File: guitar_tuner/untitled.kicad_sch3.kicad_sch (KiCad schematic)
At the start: 0 parts

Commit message: Created the audio input circuit, added all passives and assigned values
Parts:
- added C10: 470nF, symbol Device:C_Small
- added C11: 2.2uF, symbol Device:C_Small
- added C12: 10uF, symbol Device:C_Small
- added C7: 1uF, symbol Device:C_Small
- added C8: .47uF, symbol Device:C_Small
- added C9: .1uF, symbol Device:C_Small
- added MK1: Microphone, symbol Device:Microphone
- added R6: 2.21k, symbol Device:R_Small
- added R7: 150k, symbol Device:R_Small
- added R8: 100k, symbol Device:R_Small
- added R9: 1M, symbol Device:R_Small
- added U3: MAX9814, Package_DFN_QFN:DFN-14-1EP_3x3mm_P0.4mm_EP1.78x2.35mm, symbol Amplifier_Audio:MAX9814
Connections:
- new net: R6.1, R7.1, U3.13 (MICBIAS)
- new net: R7.2, R8.1, U3.14 (TH)
- new net: C10.1, U3.1 (CT)
- new net: C11.2, U3.3 (CG)
- new net: C8.2, U3.12 (BIAS)
- new net: C9.2, MK1.2 (+), R6.2
- new net: C12.1, U3.6 (MICOUT)
- new net: C9.1, U3.8 (MICIN)
- new net GND: C10.2, C11.1, C7.1, C8.1, MK1.1 (-), R8.2, R9.1, U3.11 (GND), U3.15 (GND), U3.4 (GND), U3.7 (GND), U3.9 (A/R)
- new net Vin: C7.2, U3.10 (GAIN), U3.2 (~{SHDN}), U3.5 (VDD)
- new net Vout: C12.2, R9.2

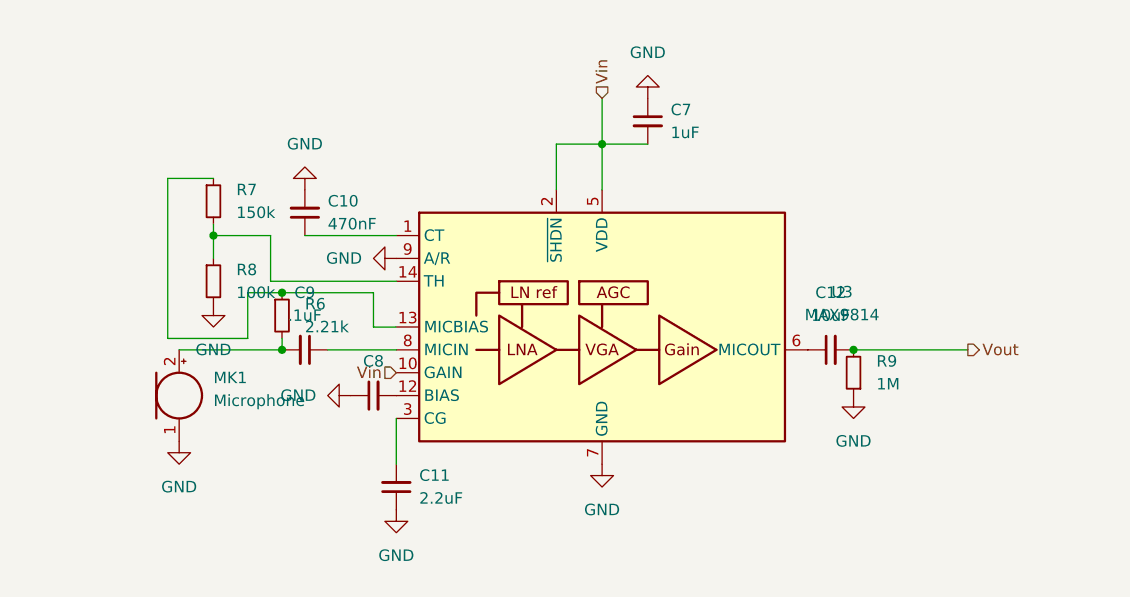
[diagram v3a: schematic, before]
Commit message: Fixed short short with R1 and space out schematic for audio input.
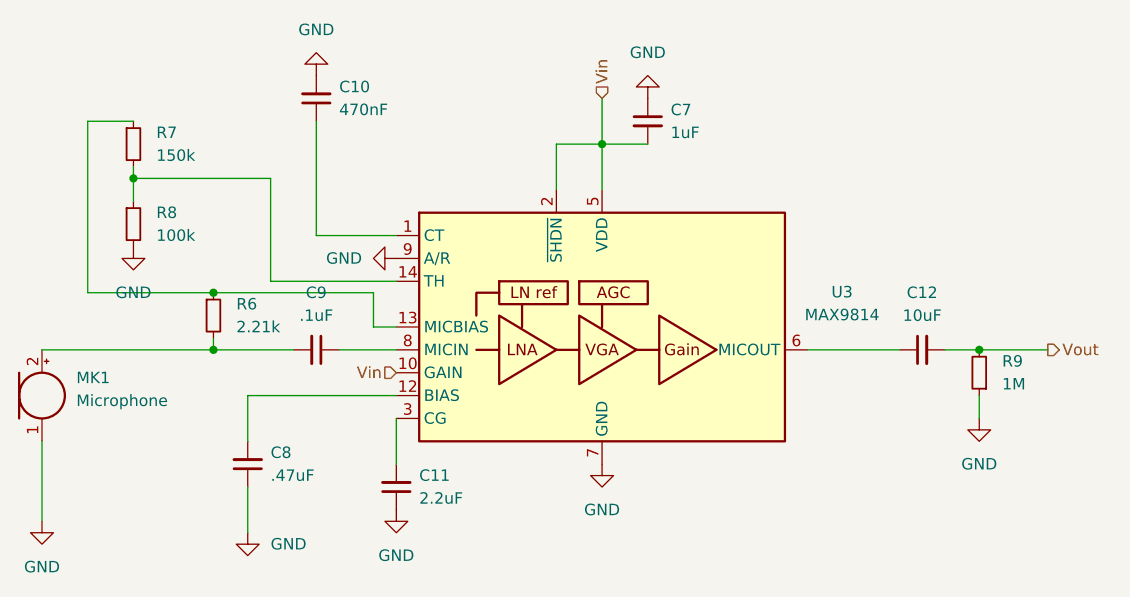
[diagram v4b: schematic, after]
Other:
- moved on the sheet: C10, C12, C8, C9, MK1, R6, R7, R8, R9

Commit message: Audio input footprints
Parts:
- C10, C11, C12, C7, C8, C9: footprint (none) -> Capacitor_SMD:C_0805_2012Metric_Pad1.18x1.45mm_HandSolder
- MK1: footprint (none) -> Inductor_THT:L_Axial_L7.0mm_D3.3mm_P2.54mm_Vertical_Fastron_MICC
- R6, R7, R8, R9: footprint (none) -> Resistor_SMD:R_0805_2012Metric_Pad1.20x1.40mm_HandSolder
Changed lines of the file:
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@@
 			)
 		)
-		(property "Footprint" ""
+		(property "Footprint" "Resistor_SMD:R_0805_2012Metric_Pad1.20x1.40mm_HandSolder"
 			(at 40.64 87.63 0)
 			(effects
@@
 			)
 		)
-		(property "Footprint" ""
+		(property "Footprint" "Capacitor_SMD:C_0805_2012Metric_Pad1.18x1.45mm_HandSolder"
 			(at 60.96 82.55 0)
 			(effects
@@
 			)
 		)
-		(property "Footprint" ""
+		(property "Footprint" "Resistor_SMD:R_0805_2012Metric_Pad1.20x1.40mm_HandSolder"
 			(at 134.62 113.03 0)
 			(effects
@@
 			)
 		)
-		(property "Footprint" ""
+		(property "Footprint" "Capacitor_SMD:C_0805_2012Metric_Pad1.18x1.45mm_HandSolder"
 			(at 69.85 125.73 0)
 			(effects
@@
 			)
 		)
-		(property "Footprint" ""
+		(property "Footprint" "Capacitor_SMD:C_0805_2012Metric_Pad1.18x1.45mm_HandSolder"
 			(at 53.34 123.19 0)
 			(effects
@@
 			)
 		)
-		(property "Footprint" ""
+		(property "Footprint" "Resistor_SMD:R_0805_2012Metric_Pad1.20x1.40mm_HandSolder"
 			(at 49.53 106.68 0)
 			(effects
@@
 			)
 		)
-		(property "Footprint" ""
+		(property "Footprint" "Capacitor_SMD:C_0805_2012Metric_Pad1.18x1.45mm_HandSolder"
 			(at 97.79 85.09 0)
 			(effects
@@
 			)
 		)
-		(property "Footprint" ""
+		(property "Footprint" "Capacitor_SMD:C_0805_2012Metric_Pad1.18x1.45mm_HandSolder"
 			(at 128.27 110.49 0)
 			(effects
@@
 			)
 		)
-		(property "Footprint" ""
+		(property "Footprint" "Capacitor_SMD:C_0805_2012Metric_Pad1.18x1.45mm_HandSolder"
 			(at 60.96 110.49 0)
 			(effects
@@
 			)
 		)
-		(property "Footprint" ""
+		(property "Footprint" "Inductor_THT:L_Axial_L7.0mm_D3.3mm_P2.54mm_Vertical_Fastron_MICC"
 			(at 30.48 113.03 90)
 			(effects
@@
 			)
 		)
-		(property "Footprint" ""
+		(property "Footprint" "Resistor_SMD:R_0805_2012Metric_Pad1.20x1.40mm_HandSolder"
 			(at 40.64 96.52 0)
 			(effects
